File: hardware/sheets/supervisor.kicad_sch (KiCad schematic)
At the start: 34 parts, among them J2 USB_HOST, J3 POST_HEX, J4 CONSOLE, J5 SWD, J6 USB_PROG, SW1 BOOTSEL, SW2 PROG SEL, U1 RP2040, U2 W25Q128JVS, U3 USBLC6-2SC6, U4 USBLC6-2SC6, Y1 12MHz

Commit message: Parts: footprints for all components, close 6 LCSC map gaps, check_parts.py
- mxsch.py emits the Footprint property from component props (was
  hard-coded empty); parts.py entries now carry a verified KiCad
  footprint, applied at build time alongside the LCSC number.
- Map keys fixed to match placed values: USB_PROG, SS34, LED (PicoGUS),
  APS6404L, CB3T3257/45 -- every combo across all sheets + cards now
  resolves (130 combos, 455 netlist components, all with footprints).
- Package corrections from JLC DB re-check: RTL8019AS is QFP-100 14x20
  P0.65 (not TQFP); C2897411 female header is a 2x10 strip -- fine for
  Core2350B, Pico needs 2x 1x20 (noted in jlcpcb-sourcing.md).
- 10 mini-xt:* placeholder footprints mark parts whose land pattern is
  authored at layout from the EasyEDA data (CH224K, magnetics, RJ45,
  HDMI, CF socket, ISA slot, switches, Core2350B PGA).
- New tools/check_parts.py: fails on unmapped combos, missing fp
  fields, or footprints absent from the installed KiCad libs.

Co-Authored-By: Claude Fable 5 <noreply@anthropic.com>
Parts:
- C1, C14, C15, C16, C17, C18, C19, C2, C20, C3, C4, C5: footprint (none) -> Capacitor_SMD:C_0603_1608Metric
- C13: footprint (none) -> Capacitor_SMD:CP_Elec_6.3x5.4
- C6: footprint (none) -> Capacitor_SMD:C_0805_2012Metric
- F1: footprint (none) -> Fuse:Fuse_1206_3216Metric
- J2: footprint (none) -> Connector_USB:USB_A_Stewart_SS-52100-001_Horizontal
- J3: footprint (none) -> Connector_PinHeader_2.54mm:PinHeader_1x10_P2.54mm_Vertical
- J4, J5: footprint (none) -> Connector_PinHeader_2.54mm:PinHeader_1x03_P2.54mm_Vertical
- J6: footprint (none) -> Connector_USB:USB_C_Receptacle_HRO_TYPE-C-31-M-12; LCSC Part Num (none) -> C2765186
- R1, R2, R3, R4, R5, R6, R7: footprint (none) -> Resistor_SMD:R_0603_1608Metric
- SW1: footprint (none) -> mini-xt:SW_TS-1187A_5.1x5.1mm
- SW2: footprint (none) -> mini-xt:SW_MST22D18G2_9.1x3.6mm
- U1: footprint (none) -> Package_DFN_QFN:QFN-56-1EP_7x7mm_P0.4mm_EP3.2x3.2mm
- U2: footprint (none) -> Package_SO:SOIC-8_5.3x5.3mm_P1.27mm
- U3, U4: footprint (none) -> Package_TO_SOT_SMD:SOT-23-6
- Y1: footprint (none) -> Crystal:Crystal_SMD_3225-4Pin_3.2x2.5mm
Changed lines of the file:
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@@
 			)
 		)
-		(property "Footprint" ""
+		(property "Footprint" "Package_DFN_QFN:QFN-56-1EP_7x7mm_P0.4mm_EP3.2x3.2mm"
 			(at 177.8 127 0)
 			(effects
@@
 			)
 		)
-		(property "Footprint" ""
+		(property "Footprint" "Crystal:Crystal_SMD_3225-4Pin_3.2x2.5mm"
 			(at 127 190.5 0)
 			(effects
@@
 			)
 		)
-		(property "Footprint" ""
+		(property "Footprint" "Capacitor_SMD:C_0603_1608Metric"
 			(at 116.84 203.2 0)
 			(effects
@@
 			)
 		)
-		(property "Footprint" ""
+		(property "Footprint" "Capacitor_SMD:C_0603_1608Metric"
 			(at 137.16 203.2 0)
 			(effects
@@
 			)
 		)
-		(property "Footprint" ""
+		(property "Footprint" "Resistor_SMD:R_0603_1608Metric"
 			(at 147.32 190.5 0)
 			(effects
@@
 			)
 		)
-		(property "Footprint" ""
+		(property "Footprint" "Resistor_SMD:R_0603_1608Metric"
 			(at 228.6 76.2 0)
 			(effects
@@
 			)
 		)
-		(property "Footprint" ""
+		(property "Footprint" "Capacitor_SMD:C_0603_1608Metric"
 			(at 241.3 76.2 0)
 			(effects
@@
 			)
 		)
-		(property "Footprint" ""
+		(property "Footprint" "Package_SO:SOIC-8_5.3x5.3mm_P1.27mm"
 			(at 279.4 76.2 0)
 			(effects
@@
 			)
 		)
-		(property "Footprint" ""
+		(property "Footprint" "Capacitor_SMD:C_0603_1608Metric"
 			(at 279.4 50.8 0)
 			(effects
@@
 			)
 		)
-		(property "Footprint" ""
+		(property "Footprint" "Resistor_SMD:R_0603_1608Metric"
 			(at 304.8 76.2 0)
 			(effects
@@
 			)
 		)
-		(property "Footprint" ""
+		(property "Footprint" "mini-xt:SW_TS-1187A_5.1x5.1mm"
 			(at 304.8 96.52 0)
 			(effects
@@
 			)
 		)
-		(property "Footprint" ""
+		(property "Footprint" "Connector_USB:USB_A_Stewart_SS-52100-001_Horizontal"
 			(at 63.5 101.6 0)
 			(effects
@@
 			)
 		)
-		(property "Footprint" ""
+		(property "Footprint" "Fuse:Fuse_1206_3216Metric"
 			(at 63.5 76.2 0)
 			(effects
@@
 			)
 		)
-		(property "Footprint" ""
+		(property "Footprint" "Resistor_SMD:R_0603_1608Metric"
 			(at 63.5 134.62 0)
 			(effects
@@
 			)
 		)
-		(property "Footprint" ""
+		(property "Footprint" "Resistor_SMD:R_0603_1608Metric"
 			(at 76.2 134.62 0)
 			(effects
@@
 			)
 		)
-		(property "Footprint" ""
+		(property "Footprint" "Package_TO_SOT_SMD:SOT-23-6"
 			(at 88.9 134.62 0)
 			(effects
@@
 			)
 		)
-		(property "Footprint" ""
+		(property "Footprint" "Capacitor_SMD:CP_Elec_6.3x5.4"
 			(at 50.8 134.62 0)
 			(effects
@@
 			)
 		)
-		(property "Footprint" ""
+		(property "Footprint" "Connector_PinHeader_2.54mm:PinHeader_1x10_P2.54mm_Vertical"
 			(at 279.4 152.4 0)
 			(effects
@@
 			)
 		)
-		(property "Footprint" ""
+		(property "Footprint" "Connector_PinHeader_2.54mm:PinHeader_1x03_P2.54mm_Vertical"
 			(at 279.4 215.9 0)
 			(effects
@@
 			)
 		)
-		(property "Footprint" ""
+		(property "Footprint" "Connector_USB:USB_C_Receptacle_HRO_TYPE-C-31-M-12"
+			(at 38.1 43.18 0)
+			(effects
+				(font
+					(size 1.27 1.27)
+				)
+				(hide yes)
+			)
+		)
+		(property "LCSC Part Num" "C2765186"
 			(at 38.1 43.18 0)
 			(effects
@@
 			)
 		)
-		(property "Footprint" ""
+		(property "Footprint" "Resistor_SMD:R_0603_1608Metric"
 			(at 88.9 43.18 0)
 			(effects
@@
 			)
 		)
-		(property "Footprint" ""
+		(property "Footprint" "Resistor_SMD:R_0603_1608Metric"
 			(at 101.6 43.18 0)
 			(effects
@@
 			)
 		)
-		(property "Footprint" ""
+		(property "Footprint" "Package_TO_SOT_SMD:SOT-23-6"
 			(at 63.5 66.04 0)
 			(effects
@@
 			)
 		)
-		(property "Footprint" ""
+		(property "Footprint" "mini-xt:SW_MST22D18G2_9.1x3.6mm"
 			(at 137.16 43.18 0)
 			(effects
@@
 			)
 		)
-		(property "Footprint" ""
+		(property "Footprint" "Connector_PinHeader_2.54mm:PinHeader_1x03_P2.54mm_Vertical"
 			(at 101.6 76.2 0)
 			(effects
@@
 			)
 		)
-		(property "Footprint" ""
+		(property "Footprint" "Capacitor_SMD:C_0603_1608Metric"
 			(at 101.6 248.92 0)
 			(effects
@@
 			)
 		)
-		(property "Footprint" ""
+		(property "Footprint" "Capacitor_SMD:C_0805_2012Metric"
 			(at 127 248.92 0)
 			(effects
@@
 			)
 		)
-		(property "Footprint" ""
+		(property "Footprint" "Capacitor_SMD:C_0603_1608Metric"
 			(at 59.69 270.51 0)
 			(effects
@@
 			)
 		)
-		(property "Footprint" ""
+		(property "Footprint" "Capacitor_SMD:C_0603_1608Metric"
 			(at 100.33 270.51 0)
 			(effects
@@
 			)
 		)
-		(property "Footprint" ""
+		(property "Footprint" "Capacitor_SMD:C_0603_1608Metric"
 			(at 139.7 270.51 0)
 			(effects
@@
 			)
 		)
-		(property "Footprint" ""
+		(property "Footprint" "Capacitor_SMD:C_0603_1608Metric"
 			(at 180.34 270.51 0)
 			(effects
@@
 			)
 		)
-		(property "Footprint" ""
+		(property "Footprint" "Capacitor_SMD:C_0603_1608Metric"
 			(at 219.71 270.51 0)
 			(effects
@@
 			)
 		)
-		(property "Footprint" ""
+		(property "Footprint" "Capacitor_SMD:C_0603_1608Metric"
 			(at 260.35 270.51 0)
 			(effects
@@
 			)
 		)
-		(property "Footprint" ""
+		(property "Footprint" "Capacitor_SMD:C_0603_1608Metric"
 			(at 299.72 270.51 0)
 			(effects

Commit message: RTC: DS12C887 sheet deleted; I2C RTC + coin cell on Supervisor
The Bus MCU now emulates ports 0x70/71 in firmware; real timekeeping moves
to a PCF8563 I2C RTC + CR2032 backup cell on the Supervisor (off-bus, synced
over the existing UART link at boot). rtc.py/rtc.kicad_sch are deleted and
"rtc" is dropped from build.py's SHEETS list (root + 12 sheets).

supervisor.py: PCF8563 (U5) on GPIO2/GPIO3 (RP2040's default I2C1 pins,
picked from the spare-GPIO pool), 4.7k pull-ups to +3V3, a two-Schottky
diode-OR (+3V3 / CR2032) onto VDD_RTC with 100nF decoupling, and the
32.768kHz crystal per the PCF8563 datasheet's single-external-cap topology
(one integrated cap on OSCO, one external trim cap on OSCI -- reused the
already-sourced 22pF rather than add a new SKU). ~{INT}/CLKOUT are NC.
RTC_SDA/RTC_SCL are supervisor-internal nets, not in PINS.

parts.py gains a 32.768kHz crystal entry (C32346, JLC's deepest-stock part,
CL=12.5pF matching the datasheet's own ceiling). bus_mcu.py gets a one-line
note on the 0x70/71 emulation and a flag that IRQ8 (previously driven by
rtc.py) is now genuinely undriven -- left as a follow-up, out of scope here.
Decisions logged in questions-supervisor.md #8.

Co-Authored-By: Claude Fable 5 <noreply@anthropic.com>
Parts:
- removed U4: USBLC6-2SC6, Package_TO_SOT_SMD:SOT-23-6, symbol Power_Protection:USBLC6-2SC6
- added BT1: CR2032, Battery:BatteryHolder_Keystone_1058_1x2032, symbol Device:Battery_Cell
- added C16, C8: 100nF, Capacitor_SMD:C_0603_1608Metric, symbol Device:C
- added C7: 22pF, Capacitor_SMD:C_0603_1608Metric, symbol Device:C
- added D1, D2: SS34, Diode_SMD:D_SMA, symbol Device:D_Schottky
- added R8, R9: 4.7k, Resistor_SMD:R_0603_1608Metric, symbol Device:R
- added U5: PCF8563T, Package_SO:SOIC-8_3.9x4.9mm_P1.27mm, symbol mini-xt:PCF8563
- added Y2: 32.768kHz, Crystal:Crystal_SMD_3215-2Pin_3.2x1.5mm, symbol Device:Crystal
- U4: renamed from C16; value 100nF -> USBLC6-2SC6; footprint Capacitor_SMD:C_0603_1608Metric -> Package_TO_SOT_SMD:SOT-23-6; symbol Device:C -> Power_Protection:USBLC6-2SC6; LCSC Part Num C14663 -> C2687116
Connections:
- net +3V3: now also U4.5 (VBUS), C16.1, D1.2 (A), R8.1, R9.1; no longer U4.1
- net GND: now also BT1.2 (-), C16.2, C7.2, C8.2, U5.4 (VSS)
- net PROG_DM: now also U4.1 (I/O1), U4.6 (I/O1)
- net PROG_DP: now also U4.3 (I/O2), U4.4 (I/O2)
- net RTC_SDA: now reaches U1.4 (GPIO2)
- net RTC_SDA: now also R8.2, U5.5 (SDA)
- net RTC_SCL: now reaches U1.5 (GPIO3)
- net RTC_SCL: now also R9.2, U5.6 (SCL)
- new net OSCI_RTC: C7.1, U5.1 (OSCI), Y2.1
- new net OSCO_RTC: U5.2 (OSCO), Y2.2
- new net VBAT_RTC: BT1.1 (+), D2.2 (A)
- new net VDD_RTC: C8.1, D1.1 (K), D2.1 (K), U5.8 (VDD)

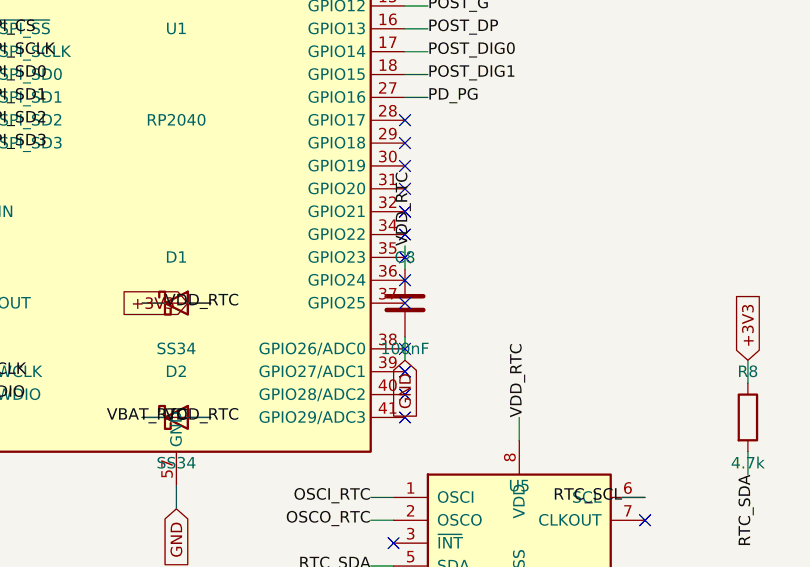
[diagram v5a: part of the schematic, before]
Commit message: ERC to zero: PWR_FLAG on VDD_RTC; retire IRQ6/IRQ8/EXT_IRQ8
Full-project ERC is now 0 errors / 0 warnings, and CLAUDE.md makes that
the standing bar. Two fixes:

- supervisor: PWR_FLAG on VDD_RTC (fed only through the D1/D2 diode-OR,
  so ERC saw no power source driving the PCF8563's VDD).
- IRQ6/IRQ8/EXT_IRQ8 formally retired (resolving the flagged IRQ8
  follow-up): none could ever be driven -- IRQ6 is a firmware floppy
  event (sidecar FDC arrives as EXT_IRQ6), IRQ8's RTC is firmware-
  emulated, EXT_IRQ8 has no header pin. Their '165 lanes tie LOW at the
  same bit positions (firmware scan map unchanged); PRIV_EXP ends at
  EXT_IRQ7; bus_mcu pulls repack 8 -> 7 full arrays. Board 405 comps /
  91 ICs. Docs + notes aligned.

Co-Authored-By: Claude Fable 5 <noreply@anthropic.com>
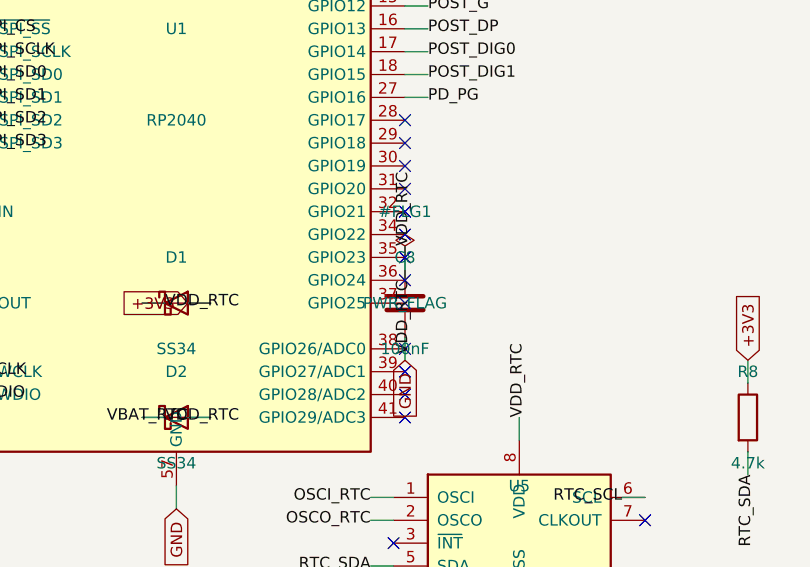
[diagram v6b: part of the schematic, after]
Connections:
- net VDD_RTC: now also U1.35 (GPIO23), U1.36 (GPIO24)
